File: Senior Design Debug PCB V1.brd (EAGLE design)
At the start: 45.4 x 17.8 mm, 38 parts, among them P00_R 1K, P01_R 1K, P02_R 1K, U1 BLE113-A-VISUAL, U2 TLV70033_DCK_5, U3 TLV70033_DCK_5

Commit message: parts laid out, ready to route
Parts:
- removed P02_LED: (no value), eagle-ltspice:LED_1206
- removed P02_R: 1K, eagle-ltspice:R0805
- removed SCL_R, SDA_R: 10K, eagle-ltspice:R0805
- moved P01_LED 98.3 mm to (38.1, 1.27), flipped to the bottom, turned to 180 degrees
- moved IMU_C4 91.5 mm to (19.7, 2.54), turned to 270 degrees
- moved P01_R 86.6 mm to (35.6, 8.26), flipped to the bottom
- moved P00_LED 86.4 mm to (33.0, 1.27), flipped to the bottom
- moved IMU_C2 82.1 mm to (27.3, 3.17), turned to 90 degrees
- moved P00_R 81.1 mm to (35.6, 5.71), flipped to the bottom
- moved IMU_C3 80.9 mm to (18.4, 5.71)
- moved SCL_PU 68.9 mm to (26.0, 12.7)
- moved OUT_C1 68.4 mm to (15.2, 8.89), turned to 90 degrees
- moved IMU_C1 66.1 mm to (17.1, 2.54), turned to 90 degrees
- moved CL_C2 58.1 mm to (19.1, 15.9), turned to 180 degrees
- moved CL_R1 51.7 mm to (14.6, 15.9)
- moved SDA_PU 47.1 mm to (21.6, 12.7)
- moved U2 12.7 mm to (14.6, 2.54), turned to 270 degrees
- moved TMR_R 11.4 mm to (10.2, 16.5), turned to 180 degrees
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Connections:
- removed net N$10: P02_LED.A, U1.P0_2
- removed net N$23: PGOOD_LED.A, PGOOD_R.1
- removed net N$24: BQ24230.9, CHG_LED.C
- removed net N$25: CHG_LED.A, CHG_R.1
- new net N$6: PGOOD_LED.C, PGOOD_R.2
- net GND: now also IMU_C4.1; no longer P02_R.1
- net IMU_PWR: no longer SCL_R.2, SDA_R.2
- net INT: now also U1.P1_2; no longer U1.P0_4
- net N$22: now also PGOOD_R.1; no longer PGOOD_LED.C
- net N$4: now also CHG_LED.C, CHG_R.2; no longer P02_LED.C, P02_R.2
- net N$5: now also BQ24230.9, CHG_R.1; no longer IMU_C4.1
- net SCL: no longer SCL_R.1
- net SDA: no longer SDA_R.1
- net VDD: now also CHG_LED.A, PGOOD_LED.A; no longer CHG_R.2, PGOOD_R.2

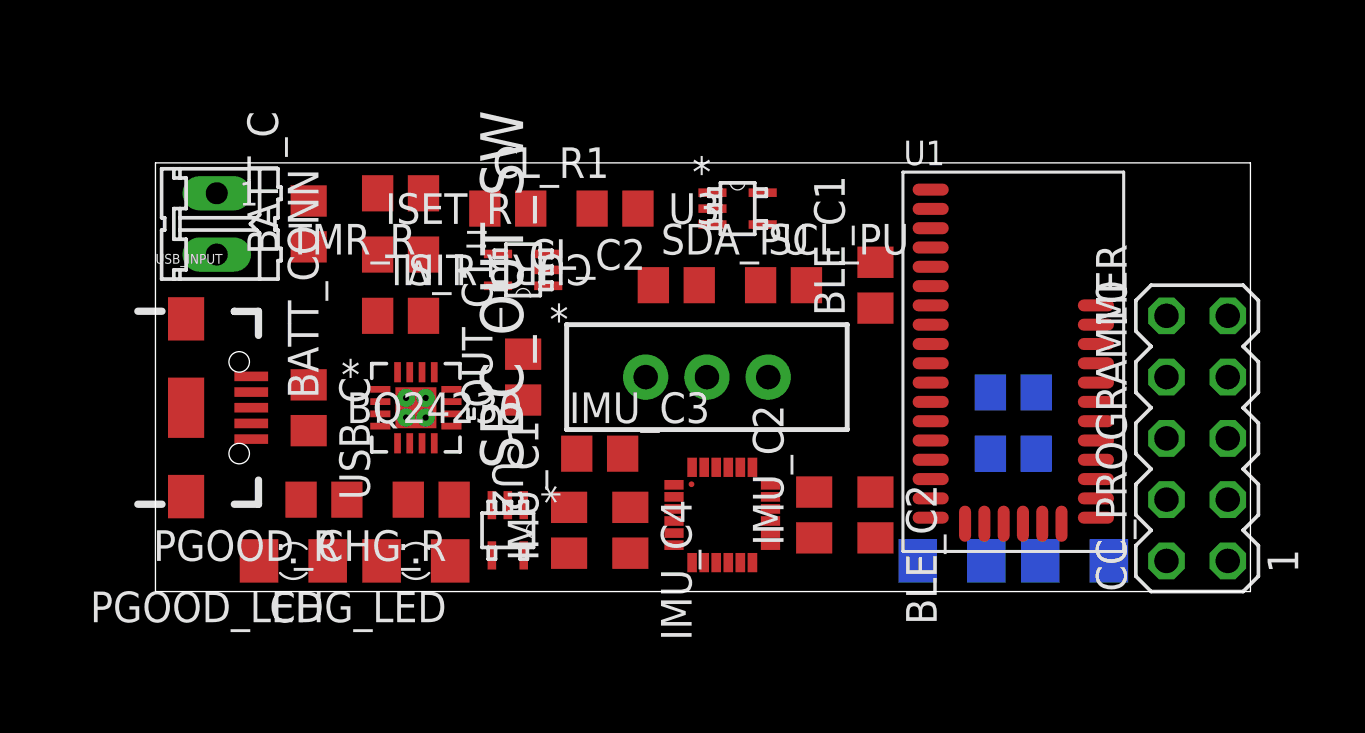
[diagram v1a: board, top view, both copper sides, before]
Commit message: finished almost all routing
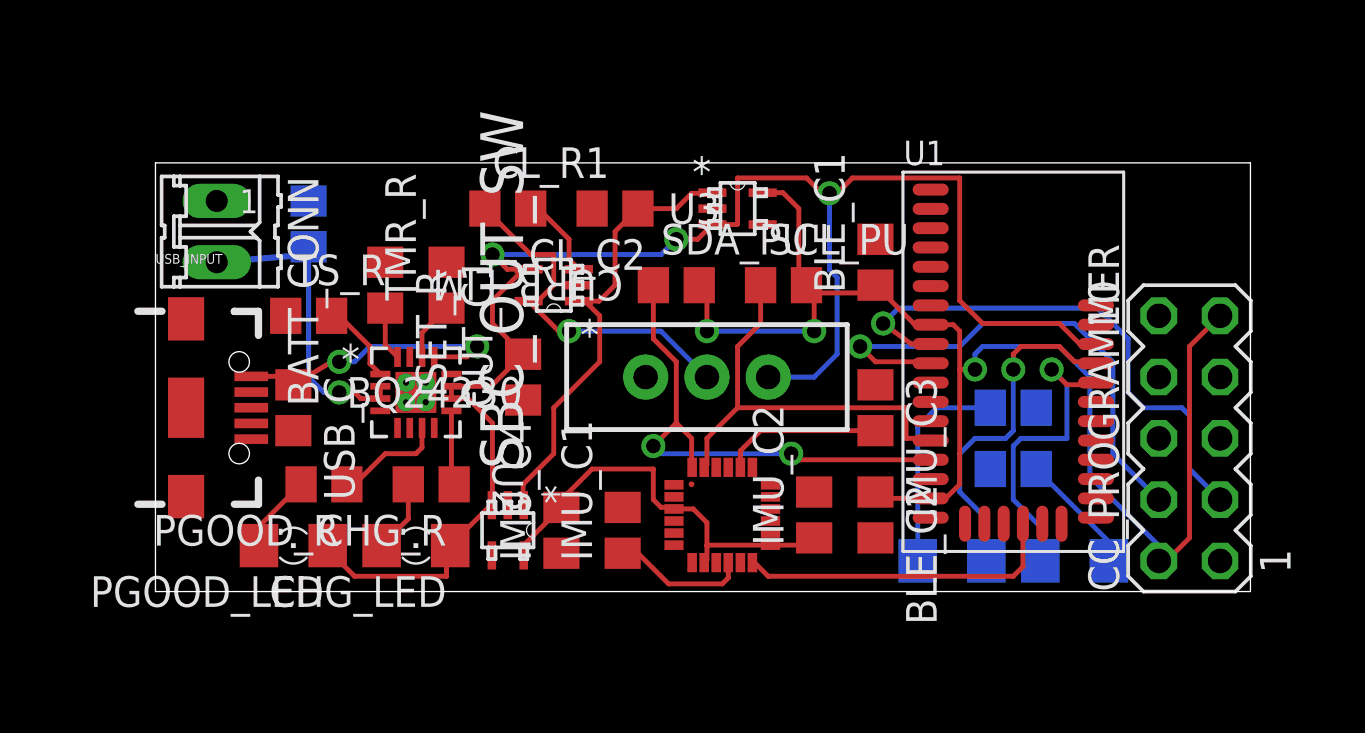
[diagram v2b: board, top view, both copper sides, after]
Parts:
- moved IMU_C3 11.6 mm to (29.8, 7.62), turned to 270 degrees
- moved TMR_R 4.26 mm to (12.1, 12.7), turned to 90 degrees
- moved TS_R 3.81 mm to (6.35, 11.4)
- moved P01_R 3.18 mm to (35.6, 5.08), turned to 180 degrees
- moved IMU_C4 2.86 mm to (16.8, 2.54), turned to 90 degrees
- moved IMU_C1 2.22 mm to (19.4, 2.54)
- moved P00_R 1.91 mm to (35.6, 7.62)
- moved CURR_LIM 1.42 mm to (16.5, 12.7)
- moved ISET_R 1.42 mm to (9.53, 12.7), turned to 270 degrees
- moved BLE_C1 0.95 mm to (29.8, 13.7)
- moved BQ24230 0.64 mm to (10.8, 8.26)
- moved CHG_R 0.64 mm to (11.4, 4.45)
- moved PGOOD_R 0.64 mm to (6.99, 4.45)
- moved CHG_LED 0.64 mm to (10.8, 1.91)
- moved PGOOD_LED 0.64 mm to (5.71, 1.91)
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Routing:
- net VDD: track 0.00 -> 69.3 mm, vias 0 -> 3
- net BLE_PWR: track 0.00 -> 57.7 mm, vias 0 -> 3
- net P2_2: track 0.00 -> 22.4 mm, vias 0 -> 1
- net P2_1: track 0.00 -> 21.6 mm, vias 0 -> 1
- net SDA: track 0.00 -> 21.3 mm, vias 0 -> 2
- net N$8: track 0.00 -> 19.0 mm
- net SCL: track 0.00 -> 17.8 mm
- net IMU_PWR: track 0.00 -> 17.5 mm
- net N$29: track 0.00 -> 14.9 mm, vias 0 -> 1
- net N$7: track 0.00 -> 14.5 mm, vias 0 -> 1
- net INT: track 0.00 -> 13.4 mm
- net N$19: track 0.00 -> 13.4 mm, vias 0 -> 1
- net N$9: track 0.00 -> 12.8 mm, vias 0 -> 1
- net DC_IN: track 0.00 -> 12.6 mm, vias 0 -> 2
- net N$14: track 0.00 -> 8.90 mm
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
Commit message: finished routing and silkscreen
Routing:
- net GND: track 0.45 -> 131.4 mm, vias 0 -> 6
- net IMU_PWR: track 17.5 -> 21.7 mm
- net N$5: track 3.09 -> 4.44 mm
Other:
- board size 45.4 x 17.8 mm -> 45.7 x 17.8 mm

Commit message: generated gerber files, deleted temp files
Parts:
- moved P00_R 9.38 mm to (27.3, 3.17), turned to 90 degrees
- moved P00_LED 6.55 mm to (35.6, 7.30)
- moved P01_R 6.02 mm to (29.8, 3.17), turned to 270 degrees
- moved P01_LED 4.58 mm to (35.6, 5.08), turned to 0 degrees
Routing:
- net GND: track 131.4 -> 208.0 mm, vias 6 -> 8
- net N$7: track 14.5 -> 6.97 mm
- net N$9: track 12.8 -> 7.96 mm
- net BLE_PWR: track 57.7 -> 62.5 mm
- net N$13: track 5.06 -> 7.50 mm
- net VDD: track 69.3 -> 68.5 mm
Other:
- board text added: "+"
- board text added: "-"
- board text added: "1"
- board text added: "10"
- board text added: "12"
- board text added: "BLE+"
- board text added: "CHG"
- board text added: "MPU+"
- board text added: "OFF"
- board text added: "ON"
- board text added: "P00"
- board text added: "P01"
- board text added: "PGOOD"
